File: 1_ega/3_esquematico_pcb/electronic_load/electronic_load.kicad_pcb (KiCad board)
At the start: 2 copper layers, 100 x 100 mm, 55 parts, among them J1 Encoder, J10 5V, J11 LOAD, J12 Memoria SD, J14 INA219, J15 VCC, J16 LCD_I2C, J17 EGB_I2C, J18 EGB_UART, J2 RTC_I2C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

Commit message: feat: pcb v2
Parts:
- removed J16: LCD_I2C, Connector_PinHeader_2.54mm:PinHeader_1x02_P2.54mm_Vertical
- removed J6: LCD_PWR, Connector_PinHeader_2.54mm:PinHeader_1x02_P2.54mm_Vertical
- added HS1: Heatsink, electronic_load:Heatsink_2725D, F.Cu at (87.5, 104.8)
- added J13: LCD, Connector_Molex:Molex_KK-254_AE-6410-04A_1x04_P2.54mm_Vertical, F.Cu at (112.4, 58.4)
- C2, C5: footprint Capacitor_THT:C_Disc_D3.4mm_W2.1mm_P2.50mm -> Capacitor_THT:C_Disc_D5.0mm_W2.5mm_P5.00mm
- C6: footprint Capacitor_THT:CP_Radial_D6.3mm_P2.50mm -> Capacitor_THT:CP_Radial_D10.0mm_P3.50mm
- L1: footprint Inductor_THT:L_Radial_D10.5mm_P5.00mm_Abacron_AISR-01 -> Inductor_THT:L_Radial_D7.5mm_P3.50mm_Fastron_07P
- SW1, SW2: footprint Connector_PinHeader_2.54mm:PinHeader_1x02_P2.54mm_Vertical -> Connector_Molex:Molex_KK-254_AE-6410-02A_1x02_P2.54mm_Vertical
- moved C5 92.3 mm to (24.5, 48.0), turned to -90 degrees
- moved J3 89.2 mm to (43.0, 114.3)
- moved C1 86.9 mm to (38.9, 40.3), turned to 0 degrees
- moved L1 86.1 mm to (27.9, 60.2), turned to 180 degrees
- moved J10 83.1 mm to (25.2, 26.3), turned to -90 degrees
- moved U2 82.3 mm to (30.8, 52.3), turned to 0 degrees
- moved R27 82.2 mm to (33.6, 27.2), turned to -90 degrees
- moved R25 77.8 mm to (34.7, 43.4), turned to 180 degrees
- moved D4 75.9 mm to (24.6, 37.4), turned to 0 degrees
- moved R24 72.5 mm to (37.2, 46.9), turned to -90 degrees
- moved R22 69.5 mm to (41.6, 46.6), turned to -90 degrees
- moved J12 63.8 mm to (111.1, 24.7)
- moved R23 61.9 mm to (42.1, 61.0), turned to 180 degrees
- moved J7 56.6 mm to (46.1, 67.6)
- moved D5 56.4 mm to (41.4, 25.5), turned to -90 degrees
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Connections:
- A1 pad 20: unconnected-(A1-GPIO15-Pad20) -> LED_ACTIVE
- A1 pad 21: I2C_SDA -> MOS_PWM
- A1 pad 22: I2C_SCL -> unconnected-(A1-GPIO17-Pad22)
- A1 pad 24: MOS_PWM -> I2C_SDA
- A1 pad 25: unconnected-(A1-GPIO19-Pad25) -> I2C_SCL
- A1 pad 26: unconnected-(A1-GPIO20-Pad26) -> RTC_SQW
- A1 pad 27: unconnected-(A1-GPIO21-Pad27) -> RTC_32K
- A1 pad 29: LED_ACTIVE -> unconnected-(A1-GPIO22-Pad29)
- C2 pad 1: Net-(U1B-+) -> Net-(U1A-+)
- R11 pad 1: Net-(U1B--) -> Net-(U1A--)
- R12 pad 2: Net-(U1B--) -> Net-(U1A--)
- R14 pad 1: Net-(U1A--) -> Net-(U1B--)
- R15 pad 1: Net-(U1A--) -> Net-(U1B--)
- R6 pad 2: Net-(U1B-+) -> Net-(U1A-+)
- SW2 pad 1: GND -> BTN_STOP
- SW2 pad 2: BTN_STOP -> GND
- U1 pad 1: TEMP_DIODE -> Net-(R11-Pad2)
- U1 pad 3: Net-(D2-A) -> Net-(U1A-+)
- U1 pad 5: Net-(U1B-+) -> Net-(D2-A)
- U1 pad 7: Net-(R11-Pad2) -> TEMP_DIODE
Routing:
- net GND: track 437.3 -> 179.3 mm
- net Net-(D2-A): track 20.4 -> 70.6 mm
- net TEMP_DIODE: track 63.2 -> 101.3 mm
- net LOAD+: track 10.8 -> 31.1 mm
- net RTC_SQW: track 0.00 -> 16.7 mm
- net Net-(U1B-+): track 14.8 -> 0.00 mm
- net Net-(Q4-E): track 23.7 -> 9.75 mm
- net VCC: track 56.6 -> 70.5 mm
- net RTC_32K: track 0.00 -> 12.9 mm
- net Net-(U1A-+): track 0.00 -> 11.2 mm
- net SPI0_CS: track 7.19 -> 18.0 mm
- net MOS_DRAIN: track 46.2 -> 57.0 mm
- net +3V3: track 123.5 -> 133.2 mm, vias 0 -> 2
- net Net-(U2-Ipk): track 34.6 -> 25.8 mm
- net RX_EGB: track 19.9 -> 11.4 mm
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
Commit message: chore: add mounting hole to pcb
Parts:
- added H1: MountingHole, MountingHole:MountingHole_3.2mm_M3_DIN965, F.Cu at (23.1, 23.1)
- added H2: MountingHole, MountingHole:MountingHole_3.2mm_M3_DIN965, F.Cu at (116.9, 23.1)
- added H3: MountingHole, MountingHole:MountingHole_3.2mm_M3_DIN965, F.Cu at (23.1, 116.9)
- added H4: MountingHole, MountingHole:MountingHole_3.2mm_M3_DIN965, F.Cu at (116.9, 116.9)
- moved D4 16.4 mm to (29.4, 21.7), turned to -90 degrees
- moved J10 6.85 mm to (25.2, 33.1)
- moved J4 6.38 mm to (80.2, 88.0), turned to 0 degrees
- moved J11 5.03 mm to (114.8, 81.5)
- moved J12 4.31 mm to (107.7, 27.3)
- moved R27 2.52 mm to (36.1, 27.9), turned to 180 degrees
- moved R25 1.00 mm to (33.8, 43.8)
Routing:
- net MOS_GATE: track 20.5 -> 32.4 mm
- net +5V: track 195.9 -> 184.8 mm
- net SPI0_RX: track 19.8 -> 15.3 mm
- net SPI0_CLK: track 20.2 -> 15.7 mm
- net SPI0_TX: track 19.9 -> 15.5 mm
- net SPI0_CS: track 18.0 -> 13.9 mm
- net GND: track 179.3 -> 175.6 mm
- net LOAD+: track 31.1 -> 29.2 mm

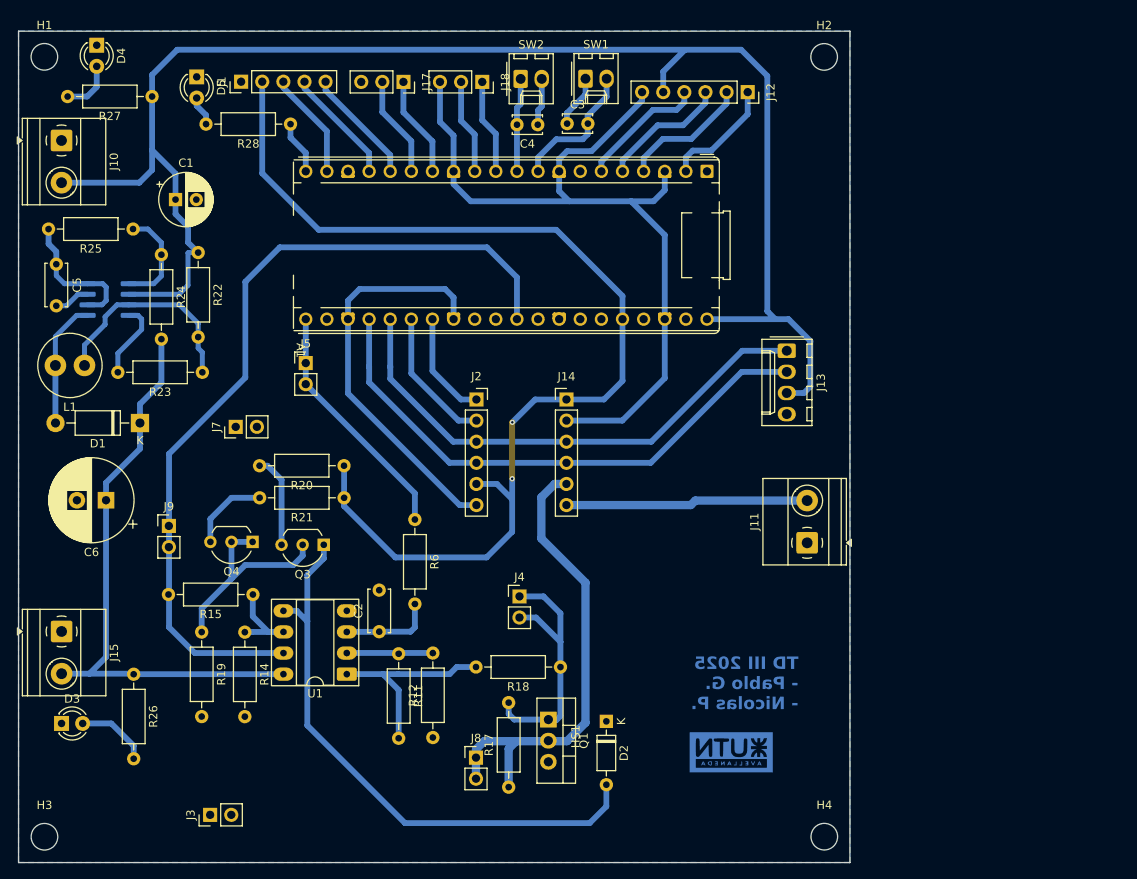
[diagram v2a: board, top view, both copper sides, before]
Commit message: minor changes to pcb MOSFET position
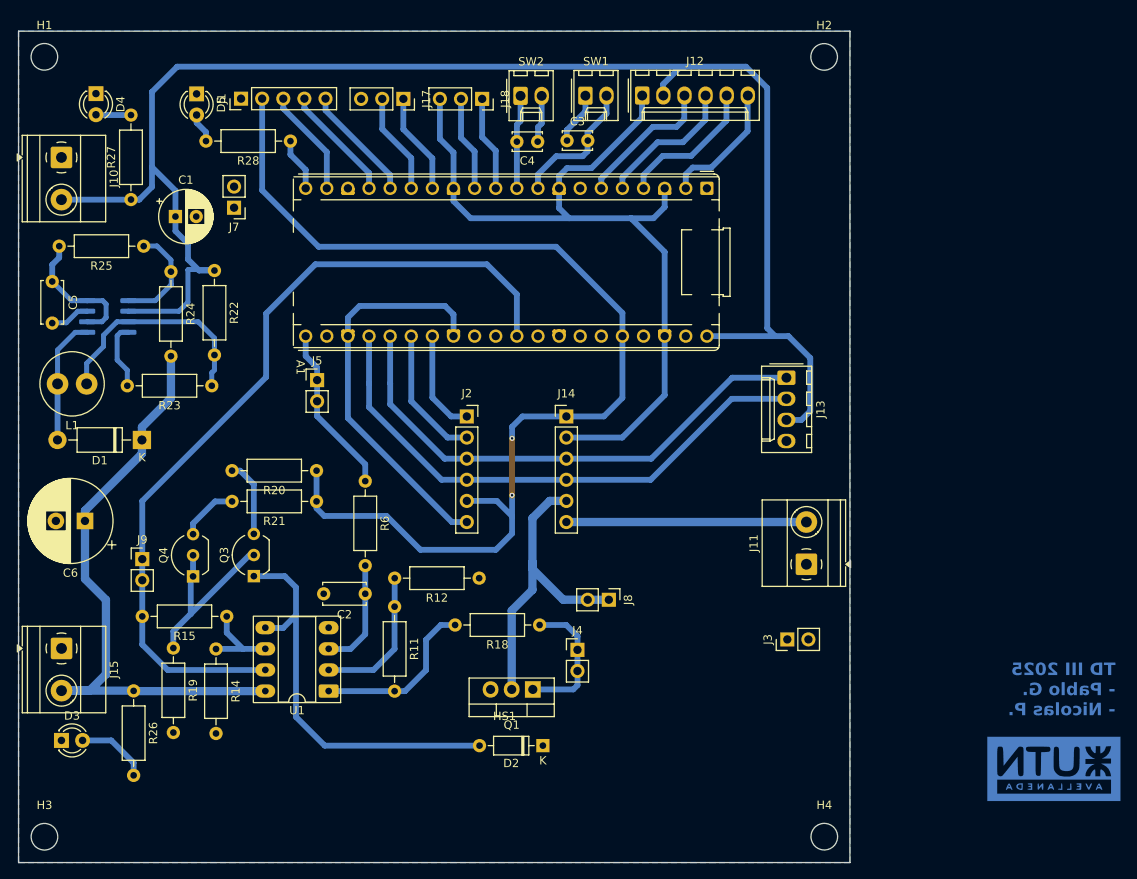
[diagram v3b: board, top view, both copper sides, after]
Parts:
- removed R17: 10k, Resistor_THT:R_Axial_DIN0207_L6.3mm_D2.5mm_P10.16mm_Horizontal
- C5: value 10nF -> 1.5nF
- J12: footprint Connector_PinSocket_2.54mm:PinSocket_1x06_P2.54mm_Vertical -> Connector_Molex:Molex_KK-254_AE-6410-06A_1x06_P2.54mm_Vertical
- L1: value 170uH -> 220 uH
- moved J3 72.6 mm to (112.5, 93.2)
- moved G*** 38.9 mm to (144.5, 108.7)
- moved J7 26.4 mm to (45.9, 41.2), turned to 180 degrees
- moved J8 24.8 mm to (91.0, 88.4), turned to -90 degrees
- moved R12 20.0 mm to (75.4, 85.8), turned to 180 degrees
- moved J12 12.7 mm to (95.0, 27.7), turned to 0 degrees
- moved R27 12.6 mm to (33.5, 40.2), turned to 90 degrees
- moved J4 9.49 mm to (87.2, 94.4)
- moved HS1 9.27 mm to (78.5, 102.9), turned to 0 degrees
- moved Q3 9.22 mm to (48.3, 85.5), turned to 90 degrees
- moved Q4 8.28 mm to (41.0, 85.6), turned to 90 degrees
- moved D2 8.17 mm to (83.1, 105.9), turned to 180 degrees
- moved R6 7.55 mm to (61.7, 74.1)
- moved D4 5.82 mm to (29.3, 27.5)
- moved R11 5.69 mm to (65.2, 89.2)
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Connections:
- J12 pad 1: SPI0_CS -> GND
- J12 pad 2: SPI0_CLK -> +5V
- J12 pad 3: SPI0_TX -> SPI0_RX
- J12 pad 4: SPI0_RX -> SPI0_TX
- J12 pad 5: +5V -> SPI0_CLK
- J12 pad 6: GND -> SPI0_CS
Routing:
- net Net-(D2-A): track 70.6 -> 49.1 mm
- net MOS_DRAIN: track 57.0 -> 38.1 mm
- net MOS_GATE: track 32.4 -> 16.6 mm
- net MOS_PWM: track 29.5 -> 20.4 mm
- net Net-(U1A--): track 10.4 -> 18.2 mm
- net +5V: track 184.8 -> 188.9 mm
- net VCC: track 70.5 -> 74.3 mm
- net Net-(Q3-B): track 26.3 -> 22.7 mm
- net Net-(R11-Pad2): track 24.5 -> 21.3 mm
- net Net-(Q4-E): track 9.75 -> 7.08 mm
- net +3V3: track 133.2 -> 135.4 mm
- net Net-(D4-A): track 6.46 -> 4.23 mm
- net Net-(U1A-+): track 11.2 -> 13.4 mm
- net SPI0_CLK: track 15.7 -> 17.3 mm
- net SPI0_CS: track 13.9 -> 15.6 mm
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
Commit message: add rtc and pcb changes
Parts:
- added F1: Fuse, Fuse:Fuseholder_Clip-5x20mm_Eaton_1A5601-01_Inline_P20.80x6.76mm_D1.70mm_Horizontal, F.Cu at (114.0, 92.5)
- moved J3 86.2 mm to (29.1, 115.1), turned to 180 degrees
- moved G*** 80.3 mm to (64.4, 113.2)
- moved J7 70.1 mm to (115.5, 33.4)
- moved J11 19.8 mm to (114.8, 104.0)
- moved J9 18.9 mm to (45.1, 67.6), turned to 90 degrees
- moved HS1 13.3 mm to (89.9, 96.1)
- moved Q1 12.2 mm to (92.2, 92.6)
- moved D2 12.1 mm to (93.0, 99.0)
- moved R18 10.1 mm to (72.8, 89.2), turned to -90 degrees
- moved J4 10.0 mm to (78.7, 89.2), turned to 90 degrees
- moved J8 9.77 mm to (100.0, 92.3), turned to 180 degrees
- moved J13 2.91 mm to (113.4, 59.0)
- moved C1 2.54 mm to (39.6, 39.9)
- moved C6 1.46 mm to (29.4, 78.9)
- moved J5 1.09 mm to (54.9, 62.3)
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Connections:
- J11 pad 2: LOAD+ -> Net-(J11-Pin_2)
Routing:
- net GND: track 176.3 -> 210.9 mm
- net Net-(J11-Pin_2): track 0.00 -> 13.5 mm
- net Net-(D2-A): track 49.1 -> 61.1 mm
- net LOAD+: track 28.9 -> 40.5 mm
- net MOS_DRAIN: track 38.1 -> 49.7 mm
- net MOS_GATE: track 16.6 -> 22.2 mm
- net Net-(R11-Pad2): track 21.3 -> 16.2 mm
- net TEMP_DIODE: track 101.2 -> 104.4 mm
- net I2C_SDA: track 66.3 -> 68.6 mm
- net I2C_SCL: track 62.6 -> 64.8 mm
- net VCC: track 74.3 -> 73.2 mm
- net Net-(Q3-B): track 22.7 -> 23.6 mm
- net Net-(U1A--): track 18.2 -> 18.9 mm
- net +3V3: track 135.4 -> 134.7 mm
- net Net-(U1A-+): track 13.4 -> 14.0 mm
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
